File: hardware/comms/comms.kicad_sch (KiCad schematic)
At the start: 0 parts

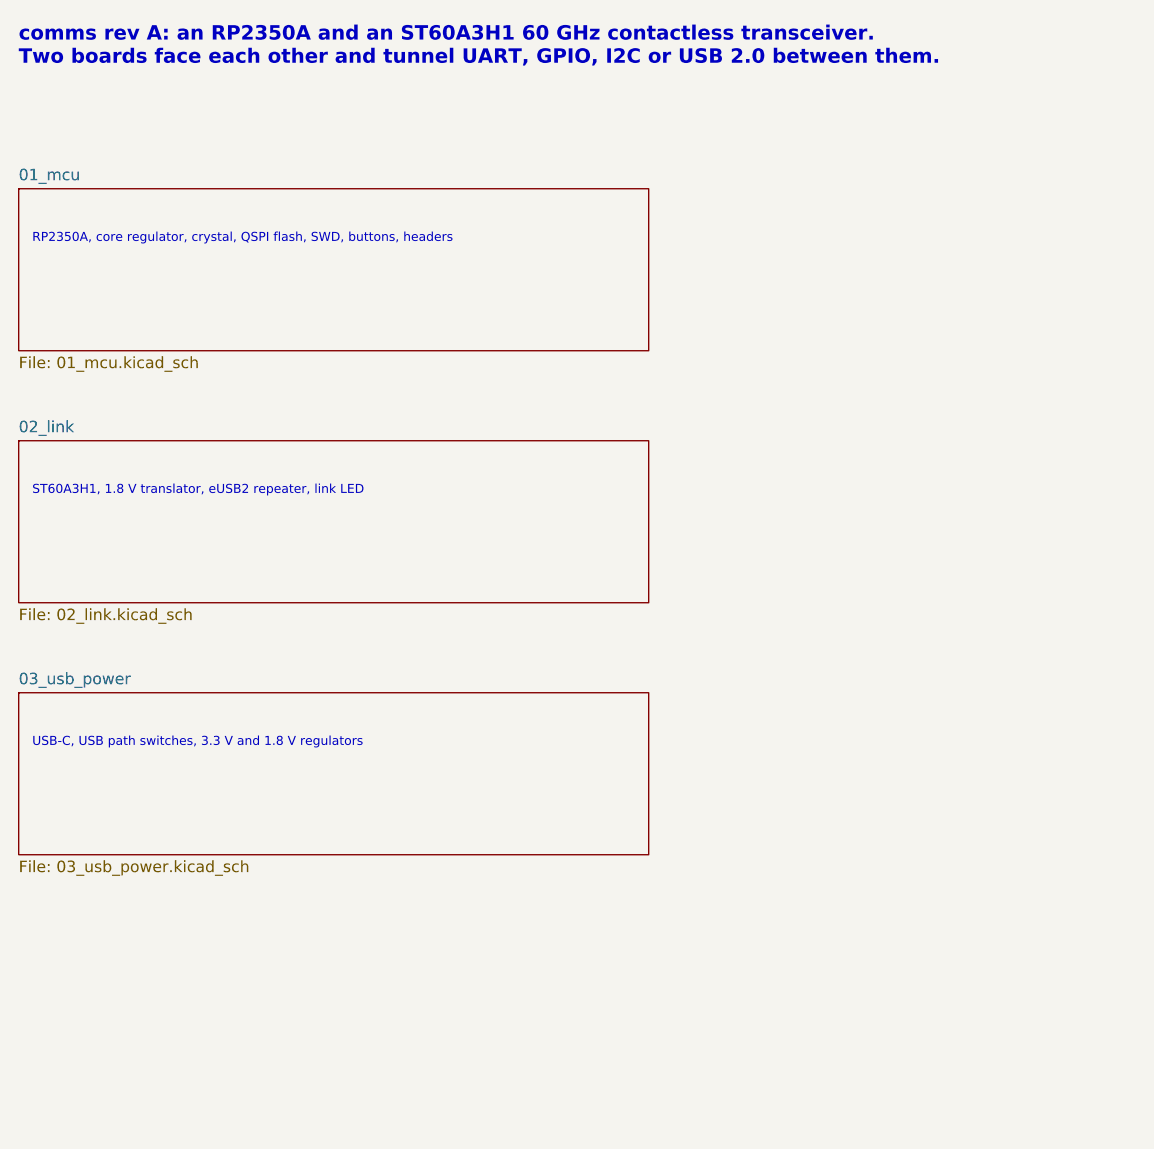
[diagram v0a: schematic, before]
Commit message: Rev B: OV2640 camera connector on the back, six layers
A 24-way flex connector (FH12-24S-0.5SH) for the common OV2640 module,
on the back of the board so the lens looks away from the link partner,
with 2.8 V and 1.3 V regulators, pull-ups and decoupling. The camera's
signals are header GPIO (0-7 data, 21 VSYNC, 22/23 SCCB, 24 PWDN,
26 HREF, 27 XCLK, 28 PCLK), wired by hand on the back from the headers'
own pads to the connector, none crossing.

Six layers (JLC06161H-7628, same outer prepreg as the four-layer stack):
with the back layer taken the board would not route on four. Parts on
the back keep their vias out of the RP2350's fan-out gaps.

An independent check confirmed the connector's pin order and contact
side against two module drawings and Hirose's data sheet, and its
findings are in: 1.3 V core, 100 n at the connector, wider supply
tracks, more room round XCLK, the module outline moved.

DRC, ERC, netlist and assembly checks pass; viewer rebuilt.

Co-Authored-By: Claude Fable 5.1 <noreply@anthropic.com>
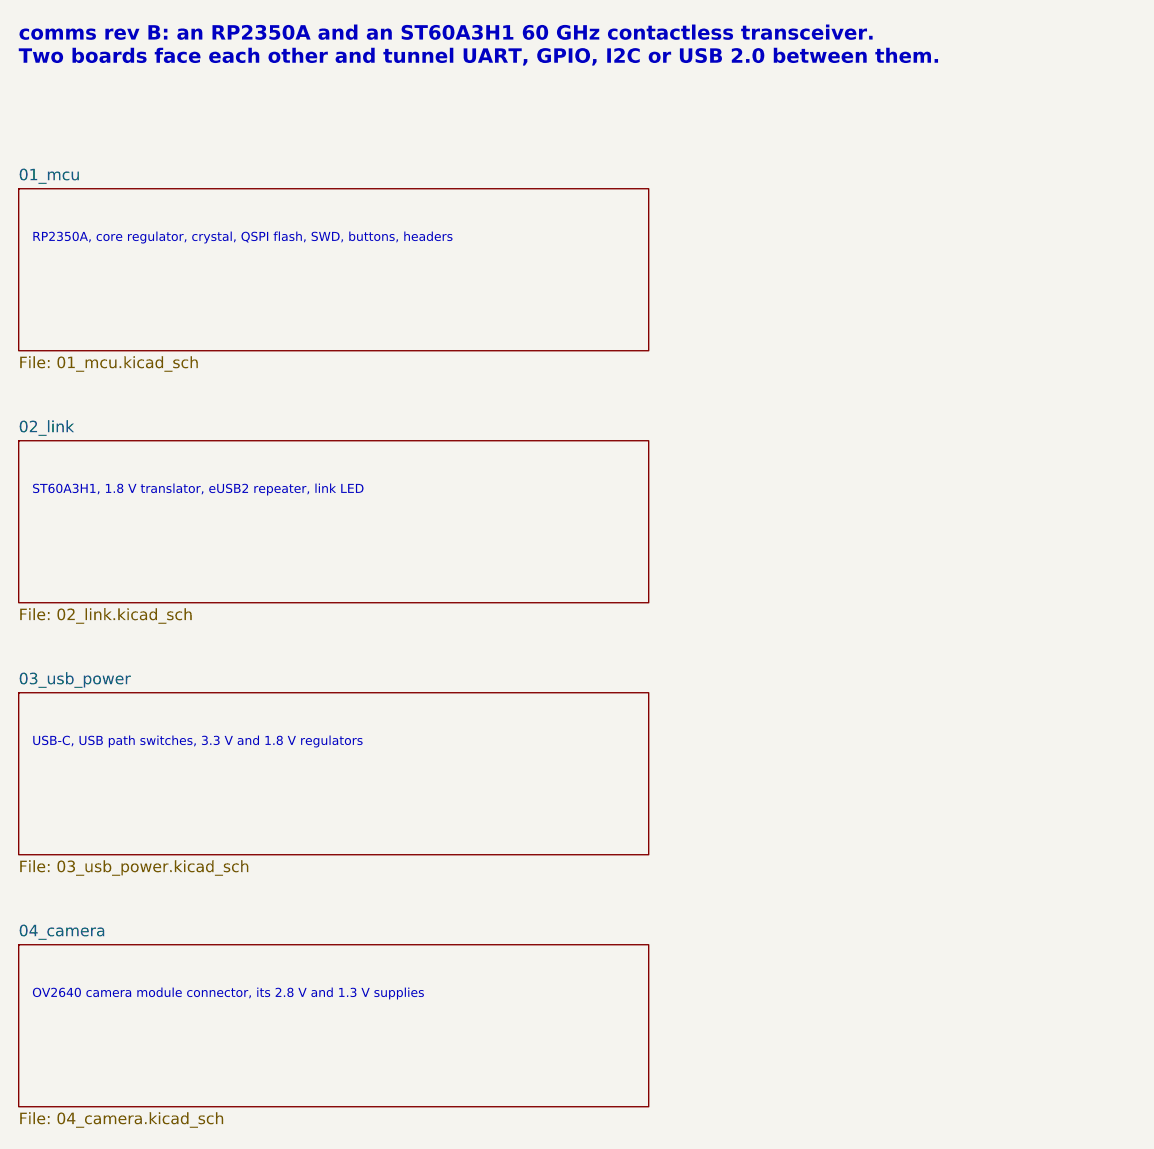
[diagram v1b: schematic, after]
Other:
- added sheet 04_camera (04_camera.kicad_sch)
- note added: "OV2640 camera module connector, its 2.8 V and 1.3 V supplies"
- note added: "comms rev B: an RP2350A and an ST60A3H1 60 GHz contactless transceiver. Two boards face each other and tunnel UART, GPIO, I2C or USB 2.0 between them."
- note removed: "comms rev A: an RP2350A and an ST60A3H1 60 GHz contactless transceiver. Two boards face each other and tunnel UART, GPIO, I2C or USB 2.0 between them."
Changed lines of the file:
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@@
 	(generator_version "9.0")
 	(paper "A4")
-	(title_block (title "comms — RP2350A + ST60A3H1 60 GHz contactless link") (date "2026-10-02") (rev "A")
+	(title_block (title "comms — RP2350A + ST60A3H1 60 GHz contactless link") (date "2026-10-02") (rev "B")
 		(company "Sequoia Hope Alexander")
 		(comment 1 "Drawn by tools/schlayout.py from the netlist in tools/circuit.py")
@@
 	(text "USB-C, USB path switches, 3.3 V and 1.8 V regulators" (exclude_from_sim no) (at 26.5 101.0 0)
 		(effects (font (size 1.0 1.0)) (justify left top)))
-	(text "comms rev A: an RP2350A and an ST60A3H1 60 GHz contactless transceiver.\nTwo boards face each other and tunnel UART, GPIO, I2C or USB 2.0 between them." (exclude_from_sim no) (at 25 22 0)
+	(sheet (at 25.0 124.0) (size 70 18)
+		(fields_autoplaced yes)
+		(stroke (width 0.1524) (type solid))
+		(fill (color 0 0 0 0.0000))
+		(property "Sheetname" "04_camera" (at 25.0 123.21 0)
+			(effects (font (size 1.27 1.27)) (justify left bottom)))
+		(property "Sheetfile" "04_camera.kicad_sch" (at 25.0 142.6 0)
+			(effects (font (size 1.27 1.27)) (justify left top)))
+		(instances (project "comms" (path "/8132f9b4-61be-5b7f-9744-e0828e24db53" (page "5"))))
+	)
+	(text "OV2640 camera module connector, its 2.8 V and 1.3 V supplies" (exclude_from_sim no) (at 26.5 129.0 0)
+		(effects (font (size 1.0 1.0)) (justify left top)))
+	(text "comms rev B: an RP2350A and an ST60A3H1 60 GHz contactless transceiver.\nTwo boards face each other and tunnel UART, GPIO, I2C or USB 2.0 between them." (exclude_from_sim no) (at 25 22 0)
 		(effects (font (size 1.6 1.6) (bold yes)) (justify left top)))
 	(sheet_instances
